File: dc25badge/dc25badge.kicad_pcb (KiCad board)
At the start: 2 copper layers, 111 parts, among them P1 BATT, P2 USB_OTG, SW1 RESET, SW2 PWR, SW3 MODE, SW4 BRIGHT, U1 MIC5305, U10 APA102, U11 APA102, U12 APA102, U13 APA102, U14 APA102, U15 APA102, U16 APA102, U17 APA102, U18 APA102, U19 APA102, U2 TPS61032, U20 APA102, U21 APA102, U22 APA102, U23 APA102, U24 APA102, U25 APA102, U26 APA102, U27 APA102, U28 APA102, U29 APA102, U3 ATSAMD21E18A-AU, U30 APA102, U31 APA102, U32 APA102, U33 APA102, U34 APA102, U35 APA102, U36 APA102, U37 APA102, U38 APA102, U39 APA102, U4 74AHCT125, U40 APA102, U41 APA102, U42 APA102, U43 APA102, U44 APA102, U45 APA102, U46 APA102, U47 APA102, U48 APA102, U49 APA102, U5 APA102, U50 APA102, U51 APA102, U52 APA102, U53 APA102, U54 APA102, U55 APA102, U56 APA102, U57 APA102, U58 APA102, U59 APA102, U6 APA102, U60 APA102, U61 APA102, U62 APA102, U63 APA102, U64 APA102, U7 APA102, U8 APA102, U9 APA102, Y1 32.768k

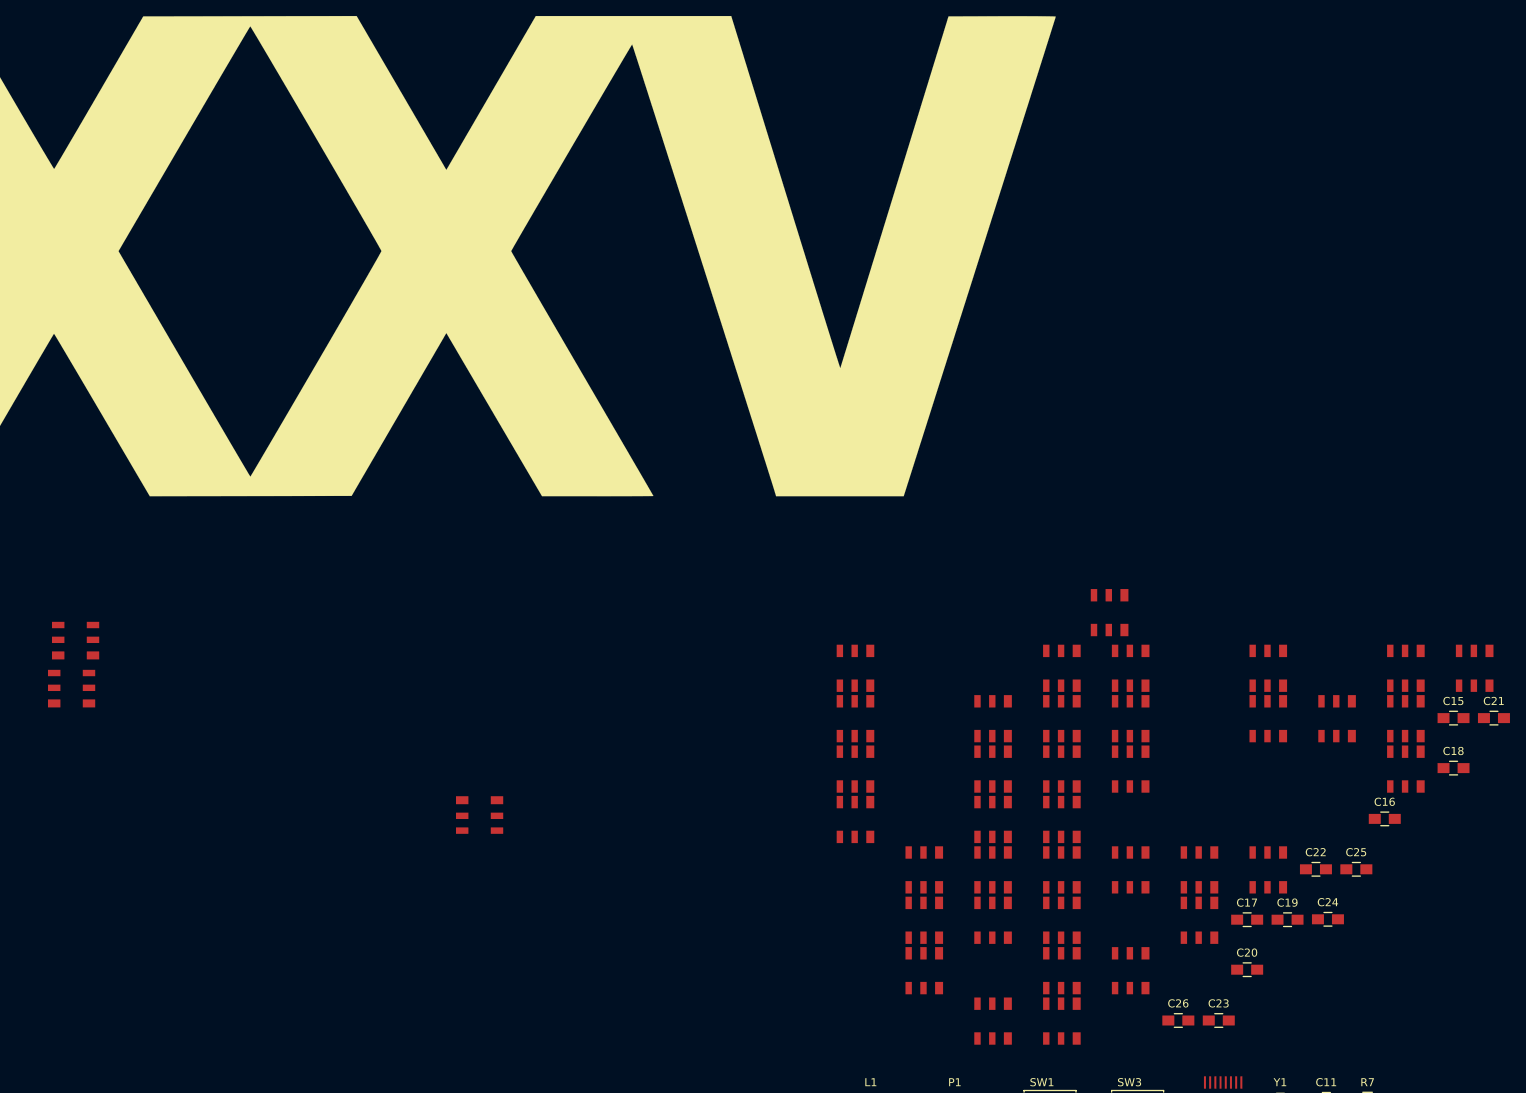
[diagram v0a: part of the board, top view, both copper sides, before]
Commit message: Layout all LEDs.
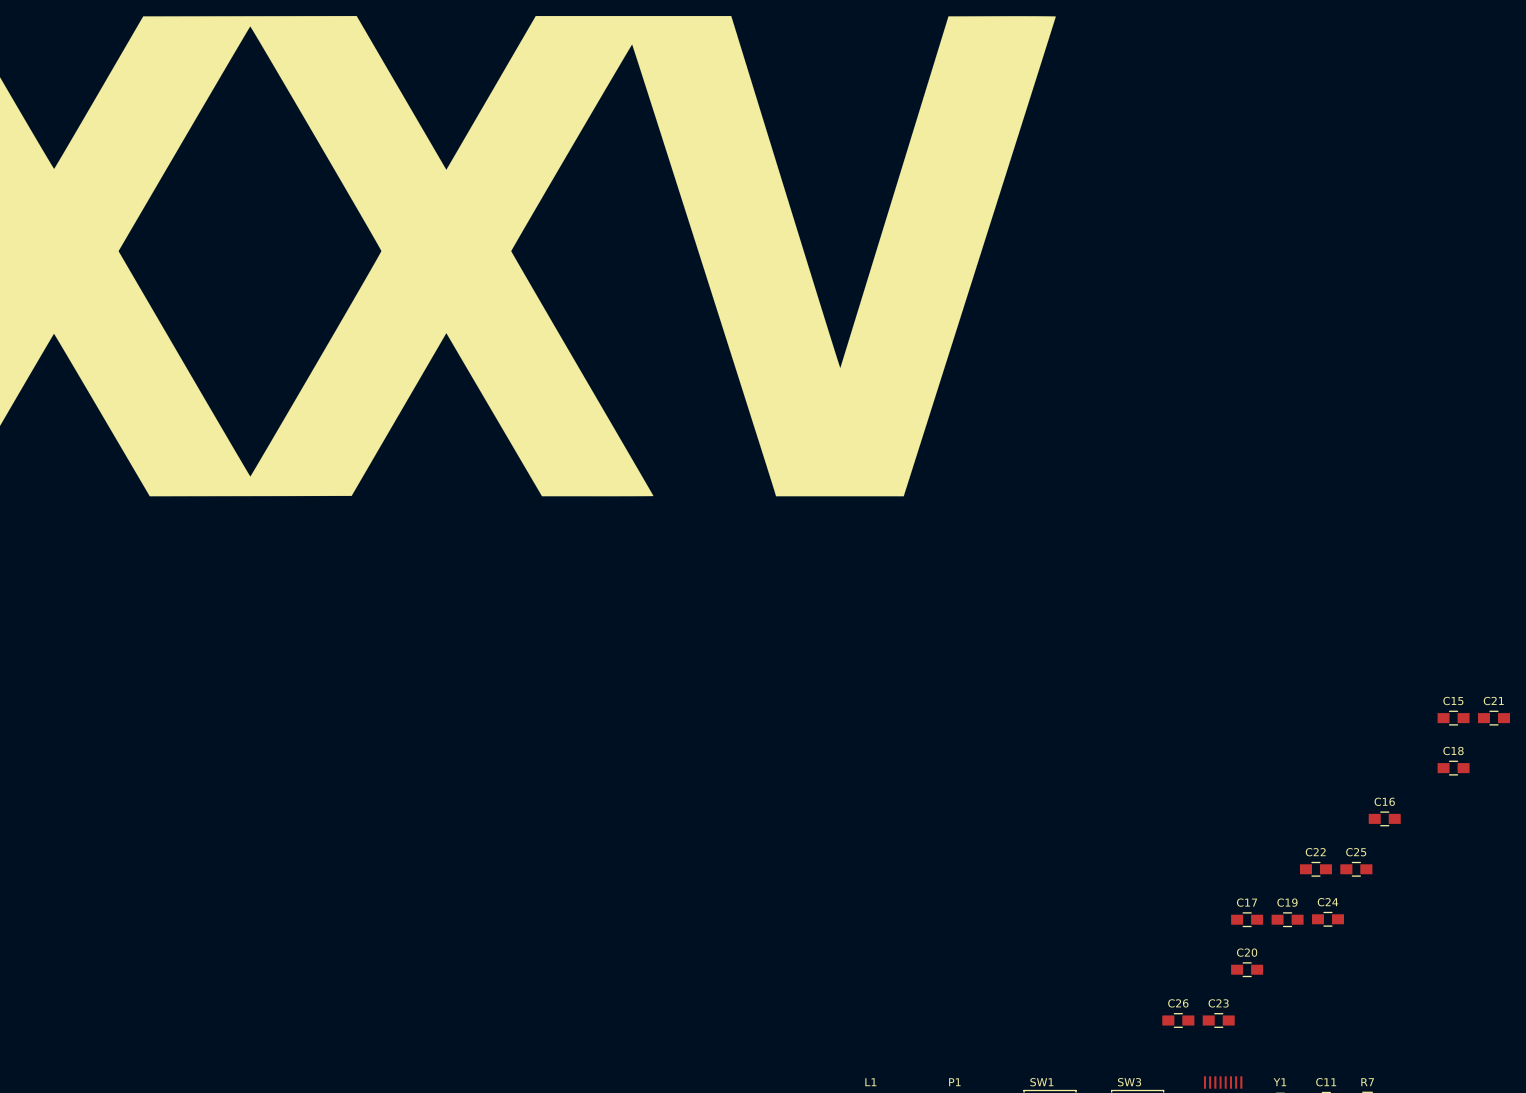
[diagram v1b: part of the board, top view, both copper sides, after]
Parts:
- moved U45 133.6 mm to (94.5, 66.0), turned to 90 degrees
- moved U15 132.6 mm to (87.5, 36.0), turned to 270 degrees
- moved U63 129.0 mm to (85.0, 84.0), turned to 90 degrees
- moved U57 124.0 mm to (88.0, 78.0), turned to 90 degrees
- moved U9 119.1 mm to (84.0, 30.0), turned to 270 degrees
- moved U48 117.8 mm to (111.5, 72.0), turned to 90 degrees
- moved U33 117.6 mm to (98.0, 54.0), turned to 270 degrees
- moved U39 116.6 mm to (98.0, 60.0), turned to 90 degrees
- moved U21 111.5 mm to (91.0, 42.0), turned to 270 degrees
- moved U27 108.5 mm to (94.5, 48.0), turned to 270 degrees
- moved U18 108.4 mm to (111.5, 42.0), turned to 270 degrees
- moved U42 106.7 mm to (108.0, 66.0), turned to 90 degrees
- moved U13 104.1 mm to (168.0, 36.0), turned to 270 degrees
- moved U24 101.4 mm to (108.0, 48.0), turned to 270 degrees
- moved U16 101.0 mm to (132.5, 36.0), turned to 270 degrees
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
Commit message: Routed 1 letter.
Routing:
- net Net-(U29-Pad1): track 0.00 -> 14.1 mm
- net Net-(U32-Pad6): track 0.00 -> 13.9 mm
- net Net-(U32-Pad5): track 0.00 -> 11.2 mm
- net Net-(U29-Pad2): track 0.00 -> 10.7 mm
- net Net-(U5-Pad6): track 0.00 -> 10.2 mm
- net Net-(U5-Pad5): track 0.00 -> 10.2 mm
- net Net-(U35-Pad2): track 0.00 -> 9.12 mm
- net Net-(U44-Pad5): track 0.00 -> 9.06 mm
- net Net-(U56-Pad5): track 0.00 -> 8.67 mm
- net Net-(U50-Pad5): track 0.00 -> 8.49 mm
- net Net-(U41-Pad2): track 0.00 -> 8.49 mm
- net Net-(U47-Pad2): track 0.00 -> 8.47 mm
- net Net-(U53-Pad2): track 0.00 -> 8.31 mm
- net Net-(U38-Pad5): track 0.00 -> 8.28 mm
- net Net-(U20-Pad5): track 0.00 -> 8.28 mm
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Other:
- net class Default: clearance 0.2 -> 0.1524; trace_width 0.25 -> 0.1524; via_dia 0.6 -> 1.016; via_drill 0.4 -> 0.508
- rule trace_clearance: 0.2 -> 0.1524
- rule trace_min: 0.2 -> 0.1524
- rule via_min_drill: 0.3 -> 0.508
- rule via_min_size: 0.4 -> 1.016

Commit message: More routing.
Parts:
- moved U56 0.51 mm to (38.5, 78.0)
- moved U62 0.51 mm to (35.0, 84.0)
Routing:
- net GND: track 0.00 -> 49.0 mm, vias 0 -> 27
- net Net-(U59-Pad2): track 0.00 -> 39.5 mm, vias 0 -> 2
- net Net-(U59-Pad1): track 0.00 -> 39.5 mm, vias 0 -> 2
- net Net-(U60-Pad2): track 0.00 -> 38.0 mm, vias 0 -> 2
- net Net-(U60-Pad1): track 0.00 -> 37.9 mm, vias 0 -> 2
- net +5V: track 0.00 -> 17.0 mm, vias 0 -> 4
- net Net-(U30-Pad1): track 0.00 -> 14.3 mm
- net Net-(U33-Pad6): track 0.00 -> 13.8 mm
- net Net-(U30-Pad2): track 0.00 -> 10.5 mm
- net Net-(U33-Pad5): track 0.00 -> 10.5 mm
- net Net-(U42-Pad2): track 0.00 -> 8.87 mm
- net Net-(U45-Pad5): track 0.00 -> 8.62 mm
- net Net-(U15-Pad2): track 0.00 -> 8.59 mm
- net Net-(U39-Pad5): track 0.00 -> 8.49 mm
- net Net-(U24-Pad2): track 0.00 -> 8.48 mm
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- added copper zone on F.Cu, net +5V
- added copper zone on B.Cu, net GND

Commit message: More more routing.
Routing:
- net GND: track 49.0 -> 73.4 mm, vias 27 -> 40
- net +5V: track 17.0 -> 34.2 mm, vias 4 -> 8
- net Net-(U32-Pad6): track 13.9 -> 14.9 mm
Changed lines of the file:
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@@
   (general
     (links 365)
-    (no_connects 282)
+    (no_connects 279)
     (area 26.344399 24.9826 234.772402 199.9424)
     (thickness 1.6)
     (drawings 0)
-    (tracks 572)
+    (tracks 632)
     (zones 0)
     (modules 111)
@@
       (xy -38.541776 -29.929667) (xy -25.203814 -29.951096) (xy -11.865852 -29.972523) (xy -6.260857 -20.357849)) (layer F.SilkS) (width 0.01))
   )
+  (segment (start 116.325 31.95) (end 114.754 31.95) (width 1.016) (layer F.Cu) (net 2) (status 400000))
+  (via (at 114.681 31.877) (size 1.016) (drill 0.508) (layers F.Cu B.Cu) (net 2))
+  (segment (start 114.754 31.95) (end 114.681 31.877) (width 1.016) (layer F.Cu) (net 2))
+  (segment (start 112.825 37.95) (end 111.148 37.95) (width 1.016) (layer F.Cu) (net 2) (status 400000))
+  (via (at 111.125 37.973) (size 1.016) (drill 0.508) (layers F.Cu B.Cu) (net 2))
+  (segment (start 111.148 37.95) (end 111.125 37.973) (width 1.016) (layer F.Cu) (net 2))
+  (segment (start 109.325 43.95) (end 107.704 43.95) (width 1.016) (layer F.Cu) (net 2) (status 400000))
+  (via (at 107.696 43.942) (size 1.016) (drill 0.508) (layers F.Cu B.Cu) (net 2))
+  (segment (start 107.704 43.95) (end 107.696 43.942) (width 1.016) (layer F.Cu) (net 2))
+  (segment (start 105.825 49.95) (end 104.306 49.95) (width 1.016) (layer F.Cu) (net 2) (status 400000))
+  (via (at 104.267 49.911) (size 1.016) (drill 0.508) (layers F.Cu B.Cu) (net 2))
+  (segment (start 104.306 49.95) (end 104.267 49.911) (width 1.016) (layer F.Cu) (net 2))
+  (segment (start 110.175 64.05) (end 108.627 64.05) (width 1.016) (layer F.Cu) (net 2) (status 400000))
+  (via (at 108.585 64.008) (size 1.016) (drill 0.508) (layers F.Cu B.Cu) (net 2))
+  (segment (start 108.627 64.05) (end 108.585 64.008) (width 1.016) (layer F.Cu) (net 2))
+  (segment (start 113.675 70.05) (end 112.087 70.05) (width 1.016) (layer F.Cu) (net 2) (status 400000))
+  (via (at 112.014 69.977) (size 1.016) (drill 0.508) (layers F.Cu B.Cu) (net 2))
+  (segment (start 112.087 70.05) (end 112.014 69.977) (width 1.016) (layer F.Cu) (net 2))
+  (segment (start 117.175 76.05) (end 115.593 76.05) (width 1.016) (layer F.Cu) (net 2) (status 400000))
+  (via (at 115.57 76.073) (size 1.016) (drill 0.508) (layers F.Cu B.Cu) (net 2))
+  (segment (start 115.593 76.05) (end 115.57 76.073) (width 1.016) (layer F.Cu) (net 2))
+  (segment (start 120.675 82.05) (end 119.134 82.05) (width 1.016) (layer F.Cu) (net 2) (status 400000))
+  (via (at 119.126 82.042) (size 1.016) (drill 0.508) (layers F.Cu B.Cu) (net 2))
+  (segment (start 119.134 82.05) (end 119.126 82.042) (width 1.016) (layer F.Cu) (net 2))
+  (segment (start 87.175 82.05) (end 88.765 82.05) (width 1.016) (layer F.Cu) (net 2) (status 400000))
+  (via (at 88.773 82.042) (size 1.016) (drill 0.508) (layers F.Cu B.Cu) (net 2))
+  (segment (start 88.765 82.05) (end 88.773 82.042) (width 1.016) (layer F.Cu) (net 2))
+  (segment (start 90.175 76.05) (end 91.798 76.05) (width 1.016) (layer F.Cu) (net 2) (status 400000))
+  (via (at 91.821 76.073) (size 1.016) (drill 0.508) (layers F.Cu B.Cu) (net 2))
+  (segment (start 91.798 76.05) (end 91.821 76.073) (width 1.016) (layer F.Cu) (net 2))
+  (segment (start 93.175 70.05) (end 94.815 70.05) (width 1.016) (layer F.Cu) (net 2) (status 400000))
+  (via (at 94.869 70.104) (size 1.016) (drill 0.508) (layers F.Cu B.Cu) (net 2))
+  (segment (start 94.815 70.05) (end 94.869 70.104) (width 1.016) (layer F.Cu) (net 2))
+  (segment (start 96.675 64.05) (end 98.256 64.05) (width 1.016) (layer F.Cu) (net 2) (status 400000))
+  (via (at 98.298 64.008) (size 1.016) (drill 0.508) (layers F.Cu B.Cu) (net 2))
+  (segment (start 98.256 64.05) (end 98.298 64.008) (width 1.016) (layer F.Cu) (net 2))
+  (segment (start 106.675 58.05) (end 108.32 58.05) (width 1.016) (layer F.Cu) (net 2) (status 400000))
+  (via (at 108.331 58.039) (size 1.016) (drill 0.508) (layers F.Cu B.Cu) (net 2))
+  (segment (start 108.32 58.05) (end 108.331 58.039) (width 1.016) (layer F.Cu) (net 2))
+  (segment (start 100.175 58.05) (end 100.225 58.05) (width 0.508) (layer F.Cu) (net 2) (status C00000))
+  (segment (start 100.225 58.05) (end 102.325 55.95) (width 0.508) (layer F.Cu) (net 2) (status C00000))
   (segment (start 53.325 55.95) (end 55.061 55.95) (width 1.016) (layer F.Cu) (net 2) (status 400000))
   (via (at 55.118 56.007) (size 1.016) (drill 0.508) (layers F.Cu B.Cu) (net 2))
@@
   (segment (start 51.175 58.05) (end 51.225 58.05) (width 0.508) (layer F.Cu) (net 2))
   (segment (start 51.225 58.05) (end 53.325 55.95) (width 0.508) (layer F.Cu) (net 2))
+  (segment (start 100.175 55.95) (end 98.609 55.95) (width 1.016) (layer F.Cu) (net 5) (status 400000))
+  (segment (start 94.118 58.05) (end 95.825 58.05) (width 1.016) (layer F.Cu) (net 5) (status 800000))
+  (segment (start 94.107 58.039) (end 94.118 58.05) (width 1.016) (layer F.Cu) (net 5))
+  (via (at 94.107 58.039) (size 1.016) (drill 0.508) (layers F.Cu B.Cu) (net 5))
+  (segment (start 96.52 58.039) (end 94.107 58.039) (width 1.016) (layer B.Cu) (net 5))
+  (segment (start 98.552 56.007) (end 96.52 58.039) (width 1.016) (layer B.Cu) (net 5))
+  (via (at 98.552 56.007) (size 1.016) (drill 0.508) (layers F.Cu B.Cu) (net 5))
+  (segment (start 98.609 55.95) (end 98.552 56.007) (width 1.016) (layer F.Cu) (net 5))
+  (segment (start 102.325 58.05) (end 104.002 58.05) (width 1.016) (layer F.Cu) (net 5) (status 400000))
+  (segment (start 108.274 55.95) (end 106.675 55.95) (width 1.016) (layer F.Cu) (net 5) (status 800000))
+  (segment (start 108.331 56.007) (end 108.274 55.95) (width 1.016) (layer F.Cu) (net 5))
+  (via (at 108.331 56.007) (size 1.016) (drill 0.508) (layers F.Cu B.Cu) (net 5))
+  (segment (start 106.045 56.007) (end 108.331 56.007) (width 1.016) (layer B.Cu) (net 5))
+  (segment (start 104.013 58.039) (end 106.045 56.007) (width 1.016) (layer B.Cu) (net 5))
+  (via (at 104.013 58.039) (size 1.016) (drill 0.508) (layers F.Cu B.Cu) (net 5))
+  (segment (start 104.002 58.05) (end 104.013 58.039) (width 1.016) (layer F.Cu) (net 5))
   (segment (start 51.175 55.95) (end 49.346 55.95) (width 1.016) (layer F.Cu) (net 5))
   (segment (start 45.223 58.05) (end 46.825 58.05) (width 1.016) (layer F.Cu) (net 5))
@@
   (segment (start 97.028 52.797) (end 95.825 54) (width 0.254) (layer F.Cu) (net 98))
   (segment (start 53.325 52.15) (end 55.071 52.15) (width 0.254) (layer F.Cu) (net 101))
-  (segment (start 54.736 61.85) (end 53.325 61.85) (width 0.1524) (layer F.Cu) (net 101))
+  (segment (start 54.736 61.85) (end 53.325 61.85) (width 0.254) (layer F.Cu) (net 101))
   (segment (start 56.388 60.198) (end 54.736 61.85) (width 0.254) (layer F.Cu) (net 101))
   (segment (start 56.388 53.467) (end 56.388 60.198) (width 0.254) (layer F.Cu) (net 101))
@@
   (segment (start 104.902 59.537598) (end 104.902 54.61) (width 0.254) (layer F.Cu) (net 104))
   (segment (start 104.439598 60) (end 104.902 59.537598) (width 0.254) (layer F.Cu) (net 104))
+  (segment (start 50.257 61.757) (end 51.082 61.757) (width 0.254) (layer F.Cu) (net 107) (status 800000))
+  (segment (start 51.082 61.757) (end 51.175 61.85) (width 0.254) (layer F.Cu) (net 107) (status C00000))
   (segment (start 51.175 52.15) (end 49.85 52.15) (width 0.254) (layer F.Cu) (net 107))
-  (segment (start 50.35 61.85) (end 51.175 61.85) (width 0.1524) (layer F.Cu) (net 107))
-  (segment (start 48 59.5) (end 50.35 61.85) (width 0.254) (layer F.Cu) (net 107))
+  (segment (start 50.35 61.85) (end 51.175 61.85) (width 0.254) (layer F.Cu) (net 107))
+  (segment (start 48 59.5) (end 50.257 61.757) (width 0.254) (layer F.Cu) (net 107))
+  (segment (start 50.257 61.757) (end 50.35 61.85) (width 0.254) (layer F.Cu) (net 107))
   (segment (start 48 54) (end 48 59.5) (width 0.254) (layer F.Cu) (net 107))
   (segment (start 49.85 52.15) (end 48 54) (width 0.254) (layer F.Cu) (net 107))

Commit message: Route all letters.
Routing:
- net GND: track 73.4 -> 106.5 mm, vias 40 -> 60
- net Net-(U43-Pad2): track 0.00 -> 7.82 mm
- net Net-(U22-Pad6): track 0.00 -> 7.73 mm
- net Net-(U13-Pad5): track 0.00 -> 7.65 mm
- net Net-(U55-Pad2): track 0.00 -> 7.64 mm
- net Net-(U52-Pad5): track 0.00 -> 7.55 mm
- net Net-(U13-Pad2): track 0.00 -> 7.51 mm
- net Net-(U37-Pad2): track 0.00 -> 7.47 mm
- net Net-(U40-Pad5): track 0.00 -> 7.44 mm
- net Net-(U49-Pad2): track 0.00 -> 7.43 mm
- net Net-(U16-Pad5): track 0.00 -> 7.40 mm
- net Net-(U19-Pad2): track 0.00 -> 7.40 mm
- net Net-(U31-Pad2): track 0.00 -> 7.39 mm
- net Net-(U58-Pad5): track 0.00 -> 7.37 mm
- net Net-(U22-Pad5): track 0.00 -> 7.35 mm
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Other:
- net class Current added: clearance 0.1524, trace_width 0.508, via_dia 1.016, via_drill 0.508
- rule trace_min: 0.1524 -> 0.254

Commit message: remove old PS.
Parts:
- removed C14, C6: 100u, Capacitors_SMD:C_1206_HandSoldering
- removed C27, C5: 1u, Capacitors_SMD:C_0805_HandSoldering
- removed C4: 10u, Capacitors_SMD:C_0805_HandSoldering
- removed L1: 6.8uH, Choke_SMD:Choke_SMD_12x12mm_h4.5mm
- removed R1: 1.8M, Resistors_SMD:R_0805_HandSoldering
- removed R2: 330k, Resistors_SMD:R_0805_HandSoldering
- removed R3, R4: 10k, Resistors_SMD:R_0805_HandSoldering
- removed U2: TPS61032, Badge_Parts:PowerPAD16
- added P3: CONN_CORTEX, Pin_Headers2:Pin_Header_Straight_2x05_Pitch1.27mm_SMD, F.Cu at (0.00, 0.00)
- added P4: UART, Pin_Headers2:Pin_Header_Straight_1x03_Pitch2.54mm_SMD_Pin1Left, F.Cu at (0.00, 0.00)
- added REF**: MountingHole_4mm, Mounting_Holes:MountingHole_4mm, F.Cu at (52.1, 33.0)
- added REF**: MountingHole_4mm, Mounting_Holes:MountingHole_4mm, F.Cu at (151.1, 33.0)
- C12, C13, U1, U3, U4, Y1: moved to B.Cu
- moved C13 185.7 mm to (64.8, 45.7), turned to 90 degrees
- moved C12 184.7 mm to (67.3, 45.7), turned to 90 degrees
- moved U4 180.5 mm to (52.1, 44.5), turned to 270 degrees
- moved Y1 179.6 mm to (66.0, 49.5)
- moved U1 175.5 mm to (77.5, 41.9), turned to 180 degrees
- moved U3 155.1 mm to (68.6, 57.1), turned to 270 degrees
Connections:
- net /VBAT renamed Net-(C1-Pad1)
- U3 pad 6: BAT_LO -> Net-(U3-Pad6)
- W3 pad 1: +5V -> Net-(W3-Pad1)

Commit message: add PS to board.
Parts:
- added C14: 22u, Capacitors_SMD:C_0805_HandSoldering, B.Cu at (144.5, 45.0)
- added C27: 22u, Capacitors_SMD:C_0805_HandSoldering, B.Cu at (146.8, 45.0)
- added C4: 22u, Capacitors_SMD:C_0805_HandSoldering, B.Cu at (156.0, 45.8)
- added C5: 0.1u, Capacitors_SMD:C_0805_HandSoldering, B.Cu at (151.3, 44.2)
- added C6: 22u, Capacitors_SMD:C_0805_HandSoldering, B.Cu at (142.2, 45.0)
- added L1: L_Core_Ferrite, Badge_Parts:Inductor_6.5x6, B.Cu at (151.3, 52.7)
- added R1: 10k, Resistors_SMD:R_0805_HandSoldering, B.Cu at (151.4, 41.7)
- added U2: TPS61232, Badge_Parts:PSON-10P, B.Cu at (151.3, 47.5)
- BRIGHT: renamed from SW4; moved to B.Cu
- CORTEX: renamed from P3; moved to B.Cu
- MODE: renamed from SW3; moved to B.Cu
- P1, P4: moved to B.Cu
- PWR: renamed from SW2; moved to B.Cu
- RESET: renamed from SW1; moved to B.Cu
- moved PWR 148.3 mm to (81.7, 67.7), turned to 180 degrees
- moved BRIGHT 146.9 mm to (81.7, 59.2), turned to 180 degrees
- moved MODE 137.9 mm to (81.7, 76.2), turned to 180 degrees
- moved P1 132.1 mm to (124.5, 41.0), turned to 90 degrees
- moved RESET 125.5 mm to (124.6, 50.2)
- moved P4 111.5 mm to (102.2, 44.5)
- moved CORTEX 91.0 mm to (69.3, 58.9)
- moved U1 19.8 mm to (96.3, 35.7)
- moved C12 17.6 mm to (81.2, 34.8)
- moved C13 17.6 mm to (78.6, 34.8)
- moved Y1 17.6 mm to (79.9, 38.6)
- moved U3 17.2 mm to (82.2, 46.6)
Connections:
- net Net-(C1-Pad1) renamed /VBAT
- W3 pad 1: Net-(W3-Pad1) -> +5V
